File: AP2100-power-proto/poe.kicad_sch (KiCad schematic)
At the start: 133 parts, among them IC2 PM8805TR, IC3 PM8804TR, J1 0826-1X1T-GH-F, J2 Barrel_Jack, Q1 BSC190N15NS3GATMA1, Q2 PBSS4240T, Q3 PBSS4240T, Q4 FDMC86259P, Q5 FOD817AS, U4 STL90N6F7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

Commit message: Cleanups per ST Micro's review. Add old and old-old kinda by accident
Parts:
- removed C116, C117: 100uF, Capacitor_SMD:CP_Elec_6.3x5.9, symbol Device:CP1_Small
- added C116: 1nF, Capacitor_SMD:C_0805_2012Metric, symbol Device:C_Small
- added C117: 47uF, Capacitor_SMD:C_1210_3225Metric, symbol Device:C_Small
- added T1, T2: RN102-2-02-1M1, Inductor_THT:Choke_Schaffner_RN102-04-14.0x14.0mm, symbol Filter:Choke_Schaffner_RN102-2-02-1M1
- C104: value 10nF -> 1.5nF; PartsBoxID 0603-10nF-X7R-100V -> 0603-1.5nF-X7R-100V
- C78: value 1nF -> 33nF; PartsBoxID 0805-1nF-X7R-250V -> 0805-33nF-X7R-100V
- C79: value 33nF -> 1nF; PartsBoxID 0805-33nF-X7R-100V -> 0805-1nF-X7R-250V
- R24: value 10K -> 10; footprint Resistor_SMD:R_0603_1608Metric -> Resistor_SMD:R_0805_2012Metric; PartsBoxID 0603-10K-1% -> 0805-10R-1%
- TR1: value POE72PR-12ED -> POE120PL-12L; footprint Scott:Transformer_Coilcraft_POE72PR -> Scott:Transformer_Coilcraft_POE120PL; symbol AP2100-rescue:Transformer_TNK_TSE265-Scott -> Scott:Transformer_POE120PL-12L; PartsBoxID POE72PR-12ED -> POE120PL-12L
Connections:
- net STBY is gone; now on net GNDPWR: IC2.3 (STBY)
- net 12V: now also C117.1
- net GND: now also C117.2
- net GNDA: now also C116.2
- net GNDPWR: now also IC2.10 (FAUX), TR1.1; no longer IC3.8 (VIN), R24.2, R28.1, TR1.5
- net VB: now also R28.1
- net at C79.1, D1.1 (A1), D2.2 (A2)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: now also T1.1; no longer C78.1, FB1.1
- net at C79.2, D1.2 (A2), D5.2 (A2)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: now also T1.3; no longer C78.2, FB2.1
- net at C83.1, D3.2 (A2), D4.1 (A1)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: now also T2.1; no longer C84.1, FB3.1
- net at C83.2, D4.2 (A2), D6.2 (A2)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: now also T2.3; no longer C84.2, FB4.1
- net at R24.1: now also IC3.8 (VIN), C116.1; no longer IC2.10 (FAUX)
- net at D11.2 (A): now also TR1.6; no longer TR1.4
- net at C110.1, C115.1, D15.1 (K)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: no longer TR1.9
- net at C109.1, D14.1 (K), R30.1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: now also TR1.8; no longer TR1.6, TR1.7
- net at C120.2, Q1.5 (D_1), Q1.6 (D_2)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: now also TR1.2; no longer TR1.3
- net at C100.1, C101.1, C102.1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: now also R24.2, TR1.5; no longer TR1.1
- new net: C78.2, FB2.1, T1.4
- new net: C78.1, FB1.1, T1.2
- new net: C84.1, FB3.1, T2.2
- new net: C84.2, FB4.1, T2.4
- no-connect marks 3 -> 4
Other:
- moved on the sheet: C109, C110, C111, C112, C113, C114, D14, D16, L10, LED5, Q2, R29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

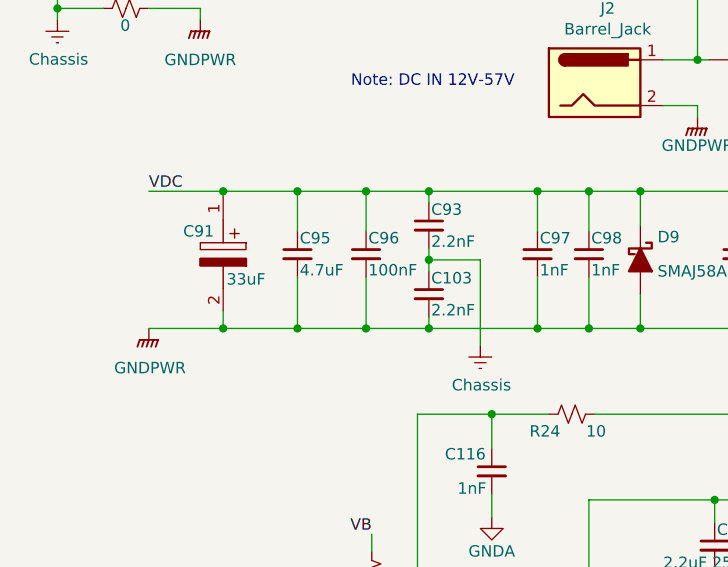
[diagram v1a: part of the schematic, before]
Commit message: Layout of PoE up to VDC - going to rework though
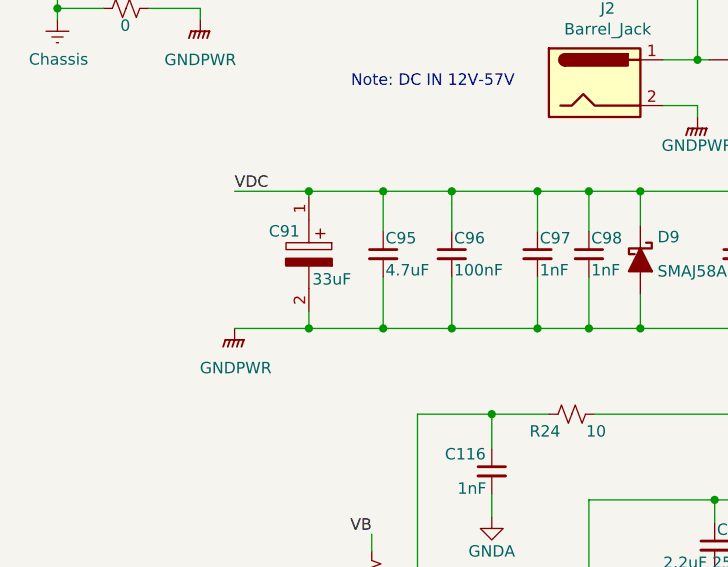
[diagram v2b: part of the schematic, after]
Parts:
- removed C103, C93: 2.2nF, Capacitor_SMD:C_1812_4532Metric, symbol Device:C_Small
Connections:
- net GND: no longer C81.1, C82.1, C86.1, C88.1, D2.1 (A1), D3.1 (A1), D5.1 (A1), D6.1 (A1), J1.21 (SHIELD), J1.22 (SHIELD), R21.2
- new net Earth: C81.1, C82.1, C86.1, C88.1, D2.1 (A1), D3.1 (A1), D5.1 (A1), D6.1 (A1), J1.21 (SHIELD), J1.22 (SHIELD), R21.2
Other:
- moved on the sheet: C91, C95, C96

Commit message: More PoE layout
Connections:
- net VDC: now also D8.2 (A); no longer D8.1 (A)
- net VOB: now also D8.1 (A); no longer D8.2 (A)
- net IN_78: now reaches C85.2, FB4.2, IC2.1 (IN78_1), IC2.40 (IN78_2), IC2.41 (IN78_3), IC2.EP1
- net IN_12: now reaches C80.1, FB1.2, IC2.12 (IN12_1), IC2.15 (IN12_2), IC2.16 (IN12_3), IC2.EP4
- net IN_36: now reaches C80.2, FB2.2, IC2.19 (IN36_1), IC2.20 (IN36_2), IC2.23 (IN36_3), IC2.EP3
- net IN_45: now reaches C85.1, FB3.2, IC2.33 (IN45_1), IC2.36 (IN45_2), IC2.37 (IN45_3), IC2.EP2
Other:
- moved on the sheet: D8
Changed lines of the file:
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@@
   (junction (at 365.125 149.225) (diameter 0.9144) (color 0 0 0 0))
   (junction (at 365.125 183.515) (diameter 0.9144) (color 0 0 0 0))
+  (no_connect (at 85.725 153.035))
   (no_connect (at 177.165 142.24))
   (no_connect (at 80.645 153.035))
-  (no_connect (at 85.725 153.035))
   (no_connect (at 90.805 191.135))
   (wire (pts (xy 48.26 45.085) (xy 52.07 45.085))
@@
     (effects (font (size 1.27 1.27)) (justify right bottom))
   )
+  (label "IN_36" (at 202.565 48.26 180)
+    (effects (font (size 1.27 1.27)) (justify right bottom))
+  )
+  (label "IN_12" (at 206.375 37.465 180)
+    (effects (font (size 1.27 1.27)) (justify right bottom))
+  )
+  (label "IN_45" (at 215.9 55.88 180)
+    (effects (font (size 1.27 1.27)) (justify right bottom))
+  )
+  (label "IN_78" (at 215.9 57.785 180)
+    (effects (font (size 1.27 1.27)) (justify right bottom))
+  )
   (label "VOB" (at 216.535 107.315 0)
     (effects (font (size 1.27 1.27)) (justify left bottom))
@@
     )
   )
-  (symbol (lib_id "Diode:BAV70") (at 290.83 90.17 180) (unit 1)
+  (symbol (lib_id "Diode:BAV70") (at 290.83 90.17 0) (mirror x) (unit 1)
     (in_bom yes) (on_board yes)
     (property "Reference" "D8" (id 0) (at 290.83 93.345 0))
